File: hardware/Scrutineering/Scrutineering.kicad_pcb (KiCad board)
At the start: 2 copper layers, 48.9 x 51.6 mm, 22 parts, among them J1 Conn_02x04, J10 Conn_01x01, J11 Conn_01x02, J12 Conn_01x02, J2 Conn_02x04, J3 Conn_01x03, J4 Conn_01x03, J5 Conn_01x01, J6 Conn_01x01, J7 Conn_01x01, J8 Conn_01x01, J9 Conn_01x01

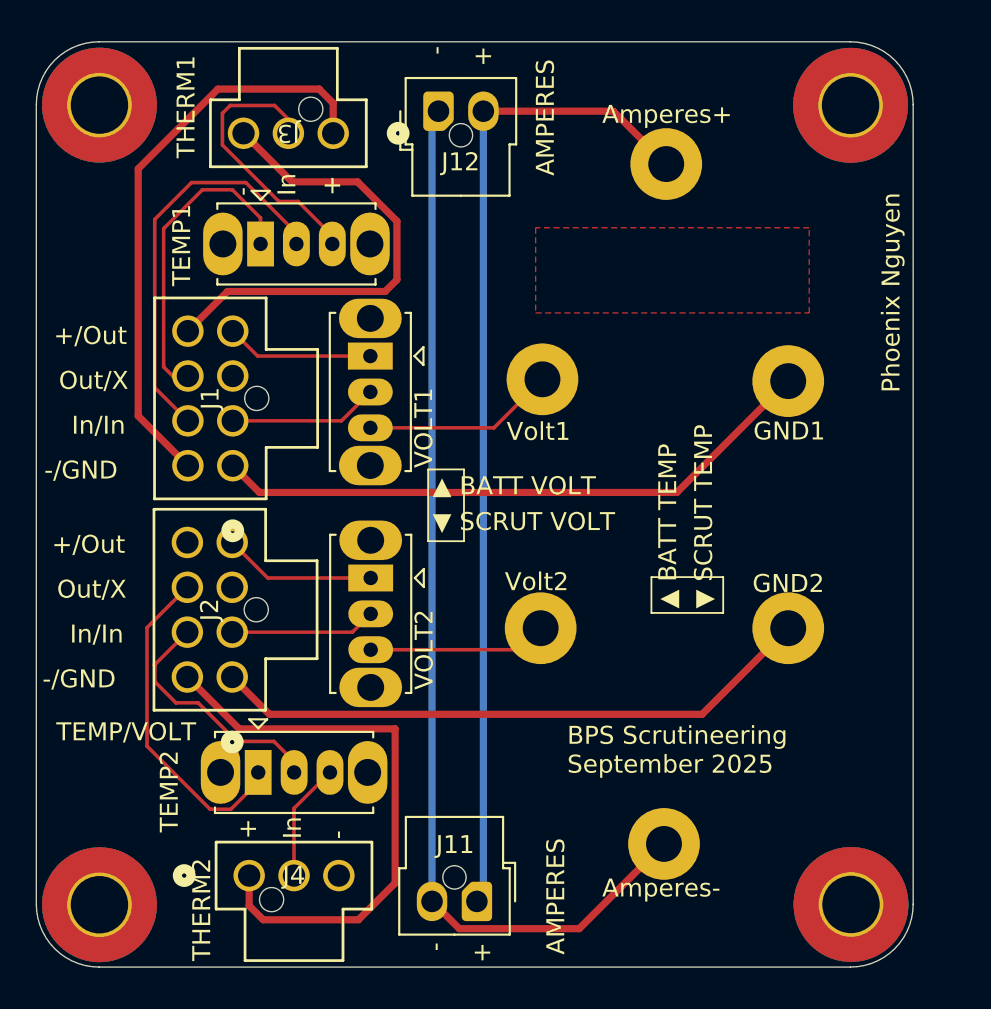
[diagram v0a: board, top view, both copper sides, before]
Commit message: Replaced Lakshay's tiny banana jacks with real ones
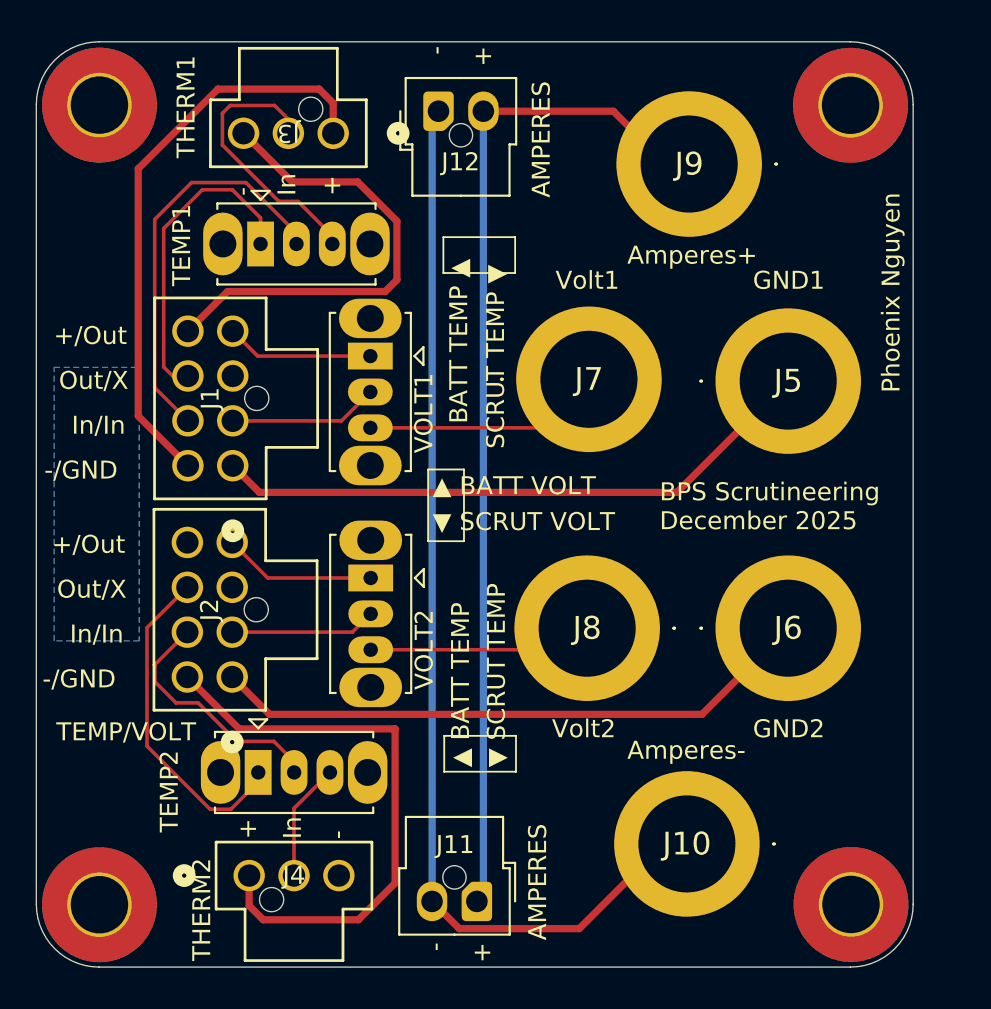
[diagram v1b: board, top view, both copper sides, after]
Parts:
- J10, J5, J6, J7, J8, J9: footprint UTSVT_Connectors:Banana_Jack_1_Pin_4mm -> VoltTemp:5754
- LOGO2: moved to B.Cu
- moved LOGO2 34.6 mm to (94.8, 78.2), turned to 90 degrees
- moved J7 2.59 mm to (122.1, 71.3)
- moved J8 2.59 mm to (122.0, 85.2)
- moved J10 1.28 mm to (127.5, 97.2)
- moved J9 1.28 mm to (127.7, 59.3)
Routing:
- net /scrutVolt7: track 10.7 -> 13.3 mm
- net /scrutVolt8: track 9.97 -> 12.6 mm
- net /scrut-: track 59.7 -> 61.0 mm
- net /scrut+: track 55.6 -> 56.9 mm
- added copper zone on B.Cu, net (none)
- removed copper zone on F.Cu, net (none)
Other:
- board text added: "BATT TEMP ▲"
- board text added: "BPS Scrutineering December 2025"
- board text added: "SCRUT TEMP ▼"
- board text removed: "BPS Scrutineering September 2025"

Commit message: fix unrouted
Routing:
- net /VDDA_8: track 0.00 -> 26.2 mm
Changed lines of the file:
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@@
 		)
 		(property "PN" ""
-			(at 0 0 -90)
+			(at 0 0 270)
 			(unlocked yes)
 			(layer "B.Fab")
@@
 		)
 		(property "p/n" ""
-			(at 0 0 -90)
+			(at 0 0 270)
 			(unlocked yes)
 			(layer "B.Fab")
@@
 		)
 		(property "Id" ""
-			(at 0 0 -90)
+			(at 0 0 270)
 			(unlocked yes)
 			(layer "B.Fab")
@@
 		)
 		(property "MANUFACTURER" ""
-			(at 0 0 -90)
+			(at 0 0 270)
 			(unlocked yes)
 			(layer "B.Fab")
@@
 		)
 		(property "MAXIMUM_PACKAGE_HEIGHT" ""
-			(at 0 0 -90)
+			(at 0 0 270)
 			(unlocked yes)
 			(layer "B.Fab")
@@
 		)
 		(property "PARTREV" ""
-			(at 0 0 -90)
+			(at 0 0 270)
 			(unlocked yes)
 			(layer "B.Fab")
@@
 		)
 		(property "STANDARD" ""
-			(at 0 0 -90)
+			(at 0 0 270)
 			(unlocked yes)
 			(layer "B.Fab")
@@
 		)
 		(property "Vds" ""
-			(at 0 0 -90)
+			(at 0 0 270)
 			(unlocked yes)
 			(layer "B.Fab")
@@
 	)
 	(segment
+		(start 99.68 80.42)
+		(end 97.75 82.35)
+		(width 0.4)
+		(layer "B.Cu")
+		(net 14)
+	)
+	(segment
+		(start 105.38505 96.25)
+		(end 108.1249 98.98985)
+		(width 0.4)
+		(layer "B.Cu")
+		(net 14)
+	)
+	(segment
+		(start 101 96.25)
+		(end 105.38505 96.25)
+		(width 0.4)
+		(layer "B.Cu")
+		(net 14)
+	)
+	(segment
+		(start 97.75 82.35)
+		(end 97.75 93)
+		(width 0.4)
+		(layer "B.Cu")
+		(net 14)
+	)
+	(segment
+		(start 97.75 93)
+		(end 101 96.25)
+		(width 0.4)
+		(layer "B.Cu")
+		(net 14)
+	)
+	(segment
